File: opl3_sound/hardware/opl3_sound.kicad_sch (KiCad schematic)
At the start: 18 parts, among them J1 8bit_thing_bus_connector, J2 Greenpak_i2c, U1 YMF262-M, U2 YAC512-M, U3 TL074, U4 SLG46826G, X1 CFPS-72 14.31818MHz

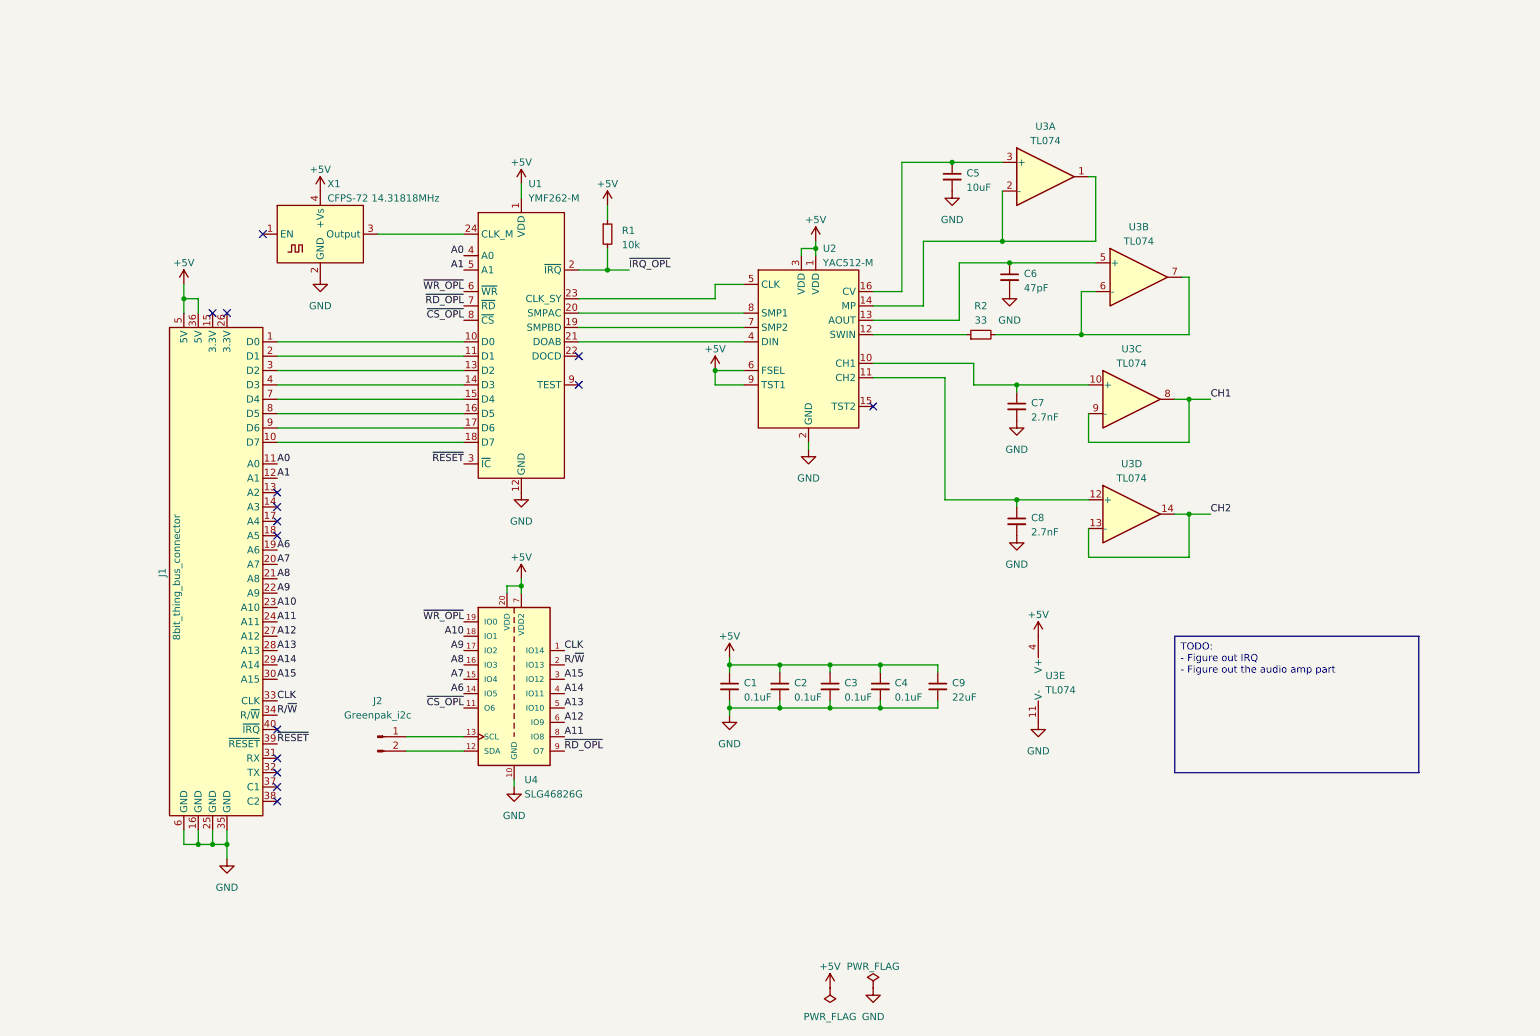
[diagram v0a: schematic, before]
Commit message: OPL3: Add LM386-based audio amplifier section to the schematic
We could use something more modern - but why not go with late 70's tech for
amplifiers too? (Ignoring the mid-90s FM chip!).
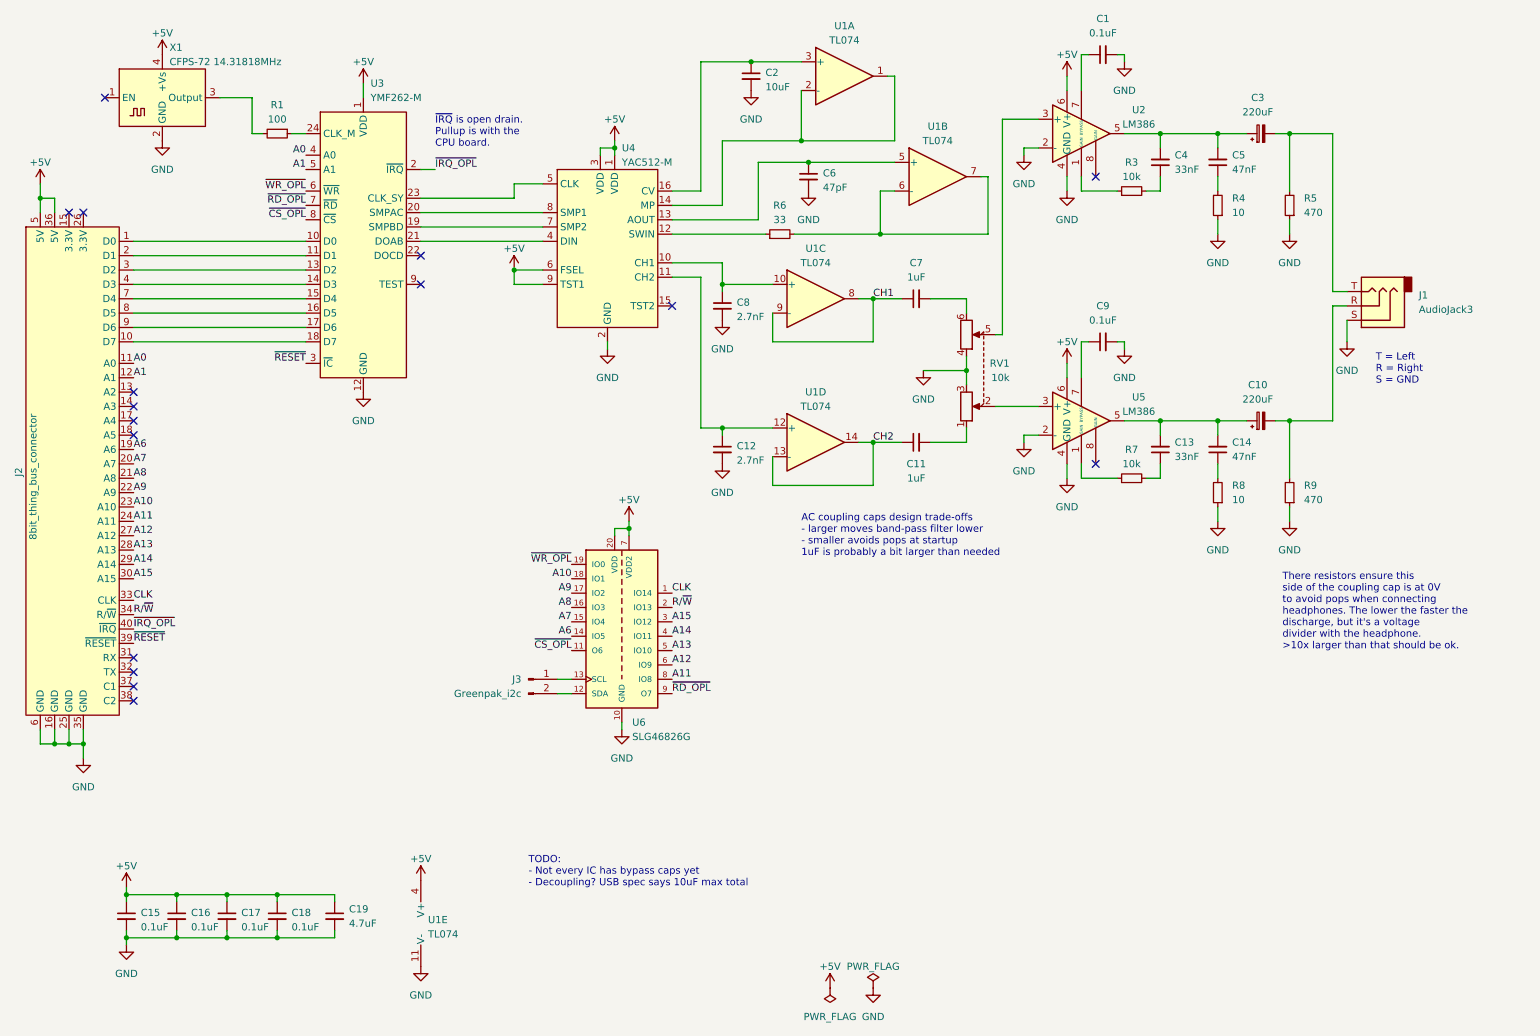
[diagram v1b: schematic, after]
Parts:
- added C1, C9: 0.1uF, symbol Device:C_Small
- added C10, C3: 220uF, symbol Device:C_Polarized_Small
- added C11, C7: 1uF, symbol Device:C_Small
- added C13, C4: 33nF, symbol Device:C_Small
- added C14, C5: 47nF, symbol Device:C_Small
- added J1: AudioJack3, symbol Connector_Audio:AudioJack3
- added R3, R7: 10k, symbol Device:R_Small
- added R4, R8: 10, symbol Device:R_Small
- added R5, R9: 470, symbol Device:R_Small
- added RV1: 10k, symbol Device:R_Potentiometer_Dual
- added U2, U5: LM386, symbol Amplifier_Audio:LM386
- C19: renamed from C9; value 22uF -> 4.7uF
- R1: value 10k -> 100
- renumbered C8 to C12, C1 to C15, C2 to C16, C3 to C17, C4 to C18, C5 to C2, C7 to C8, J1 to J2, J2 to J3, R2 to R6, U3 to U1, U1 to U3, U2 to U4, U4 to U6
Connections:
- net +5V: now also U2.6 (V+), U5.6 (V+); no longer R1.1
- net CH1: now also C7.1
- net CH2: now also C11.1
- net GND: now also C1.2, C9.2, J1.S, R4.1, R5.1, R8.1, R9.1, RV1.3, RV1.4, U2.2 (-), U2.4 (GND), U5.2 (-), U5.4 (GND)
- net ~{IRQ_OPL}: now also J2.40 (~{IRQ}); no longer R1.2
- net at U3.24 (CLK_M): now also R1.1; no longer X1.3 (Output)
- new net: C14.1, R8.2
- new net: R7.1, U5.1 (GAIN)
- new net: C13.1, R7.2
- new net: C5.1, R4.2
- new net: C3.1, C4.2, C5.2, U2.5
- new net: C3.2, J1.T, R5.2
- new net: C10.2, J1.R, R9.2
- new net: C11.2, RV1.1
- new net: RV1.2, U5.3 (+)
- new net: RV1.5, U2.3 (+)
- new net: C7.2, RV1.6
- new net: C10.1, C13.2, C14.2, U5.5
- new net: R3.1, U2.1 (GAIN)
- new net: C1.1, U2.7 (BYPASS)
- new net: C9.1, U5.7 (BYPASS)
- new net: C4.1, R3.2
- new net: R1.2, X1.3 (Output)
- no-connect marks 15 -> 16
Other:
- note added: "AC coupling caps design trade-offs - larger moves band-pass filter lower - smaller avoids pops at startup 1uF is probably a bit larger than needed"
- note added: "T = Left R = Right S = GND"
- note added: "TODO: - Not every IC has bypass caps yet - Decoupling? USB spec says 10uF max total"
- note added: "There resistors ensure this side of the coupling cap is at 0V to avoid pops when connecting headphones. The lower the faster the discharge, but it's a voltage divider with the headphone. >10x larger than that should be ok."
- note added: "~{IRQ} is open drain. Pullup is with the CPU board."
- moved on the sheet: C12, C15, C16, C17, C18, C19, C2, C6, C8, J2, J3, R6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

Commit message: Schematic / PCB / Gerbers for v2 of the OPL3 board
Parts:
- removed C1: 0.1uF, symbol Device:C_Small
- removed C13, C4: 33nF, symbol Device:C_Small
- removed C14: 47nF, symbol Device:C_Small
- removed J1: AudioJack3, symbol Connector_Audio:AudioJack3
- removed R3: 10k, symbol Device:R_Small
- removed U2, U5: LM386, symbol Amplifier_Audio:LM386
- added C10: 4.7uF, Capacitor_SMD:C_0805_2012Metric_Pad1.18x1.45mm_HandSolder, symbol Device:C_Small
- added C16: 0.68uF, Capacitor_THT:C_Rect_L7.2mm_W4.5mm_P5.00mm_FKS2_FKP2_MKS2_MKP2, symbol Device:C_Small
- added C17, C21: 4.7u, Capacitor_SMD:C_0805_2012Metric_Pad1.18x1.45mm_HandSolder, symbol Device:C_Small
- added C18, C6: 0.1uF, Capacitor_SMD:C_0805_2012Metric_Pad1.18x1.45mm_HandSolder, symbol Device:C_Small
- added J3: Headphones, Connector_Audio:Jack_3.5mm_CUI_SJ-3524-SMT_Horizontal, symbol Connector_Audio:AudioJack3_SwitchT
- added J4: Speaker, Connector_PinHeader_2.54mm:PinHeader_1x02_P2.54mm_Horizontal, symbol Connector:Conn_01x02_Pin
- added Q1: 2N7002, Package_TO_SOT_SMD:SOT-23_Handsoldering, symbol Transistor_FET:2N7002
- added R10, R11, R12, R13: 100k, Resistor_SMD:R_0805_2012Metric_Pad1.20x1.40mm_HandSolder, symbol Device:R_Small
- added R16: 0, Resistor_SMD:R_0805_2012Metric_Pad1.20x1.40mm_HandSolder, symbol Device:R_Small
- added R17: 10k, Resistor_SMD:R_0805_2012Metric_Pad1.20x1.40mm_HandSolder, symbol Device:R_Small
- added R2: 100, Resistor_SMD:R_0805_2012Metric_Pad1.20x1.40mm_HandSolder, symbol Device:R_Small
- added R5: 1k, Resistor_SMD:R_0805_2012Metric_Pad1.20x1.40mm_HandSolder, symbol Device:R_Small
- added R6, R9: 20k, Resistor_SMD:R_0805_2012Metric_Pad1.20x1.40mm_HandSolder, symbol Device:R_Small
- added U2: TLV9054, Package_SO:SOIC-14_3.9x8.7mm_P1.27mm, symbol Amplifier_Operational:TL074
- added U6: LM4880, Package_SO:SOIC-8_3.9x4.9mm_P1.27mm, symbol own_symbols:LM4880
- added U7: LM4818, Package_SO:SOIC-8_3.9x4.9mm_P1.27mm, symbol own_symbols:LM4818
- C1: renamed from C15; footprint (none) -> Capacitor_SMD:C_0805_2012Metric_Pad1.18x1.45mm_HandSolder
- C11: renamed from C19; footprint (none) -> Capacitor_SMD:C_0805_2012Metric_Pad1.18x1.45mm_HandSolder
- C12: renamed from C2; footprint (none) -> Capacitor_SMD:C_0805_2012Metric_Pad1.18x1.45mm_HandSolder
- C13: renamed from C6; footprint (none) -> Capacitor_SMD:C_0805_2012Metric_Pad1.18x1.45mm_HandSolder
- C14: renamed from C7; value 1uF -> 0.68uF; footprint (none) -> Capacitor_THT:C_Rect_L7.2mm_W4.5mm_P5.00mm_FKS2_FKP2_MKS2_MKP2
- C15: renamed from C11; value 1uF -> 0.68uF; footprint (none) -> Capacitor_THT:C_Rect_L7.2mm_W4.5mm_P5.00mm_FKS2_FKP2_MKS2_MKP2
- C19: renamed from C3; value 220uF -> 470uF; footprint (none) -> Capacitor_THT:CP_Radial_D8.0mm_P3.50mm
- C2: renamed from C16; footprint (none) -> Capacitor_SMD:C_0805_2012Metric_Pad1.18x1.45mm_HandSolder
- C20: renamed from C10; value 220uF -> 470uF; footprint (none) -> Capacitor_THT:CP_Radial_D8.0mm_P3.50mm
- C3: renamed from C17; footprint (none) -> Capacitor_SMD:C_0805_2012Metric_Pad1.18x1.45mm_HandSolder
- C4: renamed from C18; footprint (none) -> Capacitor_SMD:C_0805_2012Metric_Pad1.18x1.45mm_HandSolder
- C5: value 47nF -> 0.1uF; footprint (none) -> Capacitor_SMD:C_0805_2012Metric_Pad1.18x1.45mm_HandSolder
- C7: renamed from C8; footprint (none) -> Capacitor_SMD:C_0805_2012Metric_Pad1.18x1.45mm_HandSolder
- C8: renamed from C12; footprint (none) -> Capacitor_SMD:C_0805_2012Metric_Pad1.18x1.45mm_HandSolder
- C9: value 0.1uF -> 4.7uF; footprint (none) -> Capacitor_SMD:C_0805_2012Metric_Pad1.18x1.45mm_HandSolder
- J2: renamed from J3; footprint (none) -> own_footprints:PinHeader_1x02_P2.54mm_Vertical_minimal
- R1: footprint (none) -> Resistor_SMD:R_0805_2012Metric_Pad1.20x1.40mm_HandSolder
- R14: renamed from R5; value 470 -> 1k; footprint (none) -> Resistor_SMD:R_0805_2012Metric_Pad1.20x1.40mm_HandSolder
- R15: renamed from R9; value 470 -> 1k; footprint (none) -> Resistor_SMD:R_0805_2012Metric_Pad1.20x1.40mm_HandSolder
- R3: renamed from R6; footprint (none) -> Resistor_SMD:R_0805_2012Metric_Pad1.20x1.40mm_HandSolder
- R4: value 10 -> 1k; footprint (none) -> Resistor_SMD:R_0805_2012Metric_Pad1.20x1.40mm_HandSolder
- R7: value 10k -> 20k; footprint (none) -> Resistor_SMD:R_0805_2012Metric_Pad1.20x1.40mm_HandSolder
- R8: value 10 -> 100k; footprint (none) -> Resistor_SMD:R_0805_2012Metric_Pad1.20x1.40mm_HandSolder
- RV1: footprint (none) -> imported_footprints:PTD9022015KA104
- U1: value TL074 -> TLV9054; footprint (none) -> Package_SO:SOIC-14_3.9x8.7mm_P1.27mm
- U3: renamed from U6; footprint SOP65P640X120-20N -> imported_footprints:SOP65P640X120-20N
- U5: renamed from U4; footprint Package_SO:SO-16_5.3x10.2mm_P1.27mm -> Package_SO:SOIC-16W_5.3x10.2mm_P1.27mm
- X1: footprint Oscillator:Oscillator_SMD_IQD_IQXO70-4Pin_7.5x5.0mm -> Oscillator:Oscillator_SMD_IQD_IQXO70-4Pin_7.5x5.0mm_HandSoldering
- renumbered J2 to J1, U3 to U4
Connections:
- net +5V: now also C5.1, C9.1, R8.2, C10.1, C6.1, R13.2, U2.4 (V+), U6.8 (VDD), U7.6 (VDD)
- net CH1: now also RV1.3, U1.1, U1.2 (-); no longer C14.1, U1.8, U1.9 (-)
- net CH2: now also RV1.6, U1.6 (-), U1.7; no longer C15.1, U1.13 (-), U1.14
- net GND: now also C5.2, C10.2, C17.2, C18.1, C21.2, C6.2, J3.S, Q1.2 (S), R17.2, U2.11 (V-), U6.4 (GND), U7.7 (GND); no longer R4.1, R8.1, RV1.3, RV1.4
- net ~{CS_OPL}: now also U3.19 (IO0); no longer U3.11 (O6)
- net ~{WR_OPL}: now also U3.11 (O6); no longer U3.19 (IO0)
- net at R7.1: now also C15.2
- net at R7.2: now also R11.2, U6.6 (INB)
- net at R4.2: now also C16.1, R5.2; no longer C5.1
- net at C19.1: now also R10.2, U6.1 (OUTA); no longer C5.2
- net at C7.1, U5.10 (CH1): now also U1.3 (+); no longer U1.10 (+)
- net at C19.2, R14.2: now also J3.T
- net at C20.2, R15.2: now also J3.R
- net at C8.1, U5.11 (CH2): now also U1.5 (+); no longer U1.12 (+)
- net at RV1.1: now also RV1.4, R2.1; no longer C15.2
- net at RV1.2: now also U2.3 (+), U2.5 (+)
- net at RV1.5: now also U2.10 (+), U2.12 (+)
- net at C14.2: now also R6.1; no longer RV1.6
- net at C20.1: now also R11.1, U6.7 (OUTB)
- net at C13.1, U5.13 (AOUT): now also U1.12 (+); no longer U1.5 (+)
- net at C12.1, U5.16 (CV): now also U1.10 (+); no longer U1.3 (+)
- new net: R4.1, U2.6 (-), U2.7
- new net: R2.2, U1.8, U1.9 (-), U5.14 (MP)
- new net: R5.1, U2.8, U2.9 (-)
- new net: C15.1, U2.13 (-), U2.14
- new net: C17.1, U6.3 (BYPASS)
- new net: C21.1, U7.2 (BYPASS)
- new net: C16.2, R9.1
- new net: R12.1, R16.1
- new net: R12.2, R9.2, U7.4 (IN-)
- new net: C14.1, U2.1, U2.2 (-)
- new net: Q1.3 (D), R8.1, U6.5 (SHUTDOWN)
- new net: R10.1, R6.2, U6.2 (INA)
- new net: C18.2, U7.3 (IN+)
- new net: J4.2 (Pin_2), R16.2, U7.5 (VO1)
- new net: J4.1 (Pin_1), U7.8 (VO2)
- new net: R3.2, U1.13 (-), U1.14
- new net SPEAKER_SHUTDOWN: J3.TN, Q1.1 (G), R13.1, R17.1, U7.1 (SHUTDOWN)
- no-connect marks 16 -> 14
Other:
- note added: "Pulldown if the headphone jack is not populated"
- note removed: "AC coupling caps design trade-offs - larger moves band-pass filter lower - smaller avoids pops at startup 1uF is probably a bit larger than needed"
- note removed: "TODO: - Not every IC has bypass caps yet - Decoupling? USB spec says 10uF max total"
- note removed: "There resistors ensure this side of the coupling cap is at 0V to avoid pops when connecting headphones. The lower the faster the discharge, but it's a voltage divider with the headphone. >10x larger than that should be ok."
- title: (none) -> OPL3 Sound
- moved on the sheet: C1, C11, C12, C13, C14, C15, C19, C2, C20, C3, C4, C7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

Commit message: Update OPL3 board schematics for lower amplification settings
The 5x for both speaker and headphones is too much. It's now 1.3 and no
amplification at all.
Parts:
- R10, R11: value 100k -> 20k
- R12: value 100k -> 33k
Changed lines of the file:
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@@
       (effects (font (size 1.27 1.27)))
     )
-    (property "Value" "100k" (at 234.95 118.11 90)
+    (property "Value" "33k" (at 234.95 118.11 90)
       (effects (font (size 1.27 1.27)))
     )
@@
       (effects (font (size 1.27 1.27)))
     )
-    (property "Value" "100k" (at 220.98 55.88 90)
+    (property "Value" "20k" (at 220.98 55.88 90)
       (effects (font (size 1.27 1.27)))
     )
@@
       (effects (font (size 1.27 1.27)))
     )
-    (property "Value" "100k" (at 220.98 110.49 90)
-      (effects (font (size 1.27 1.27)))
-    )
+    (property "Value" "20k" (at 220.98 110.49 90)
+      (effects (font (size 1.27 1.27)))
+    )
